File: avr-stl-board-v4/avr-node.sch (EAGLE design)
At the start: 36 parts, among them IC2 DS1307, IC3 LM358N, Q1 32.768kHz, Q3 16MHz, T1 S8050, U1 24LC256, U3 ATMEGA328P-PU

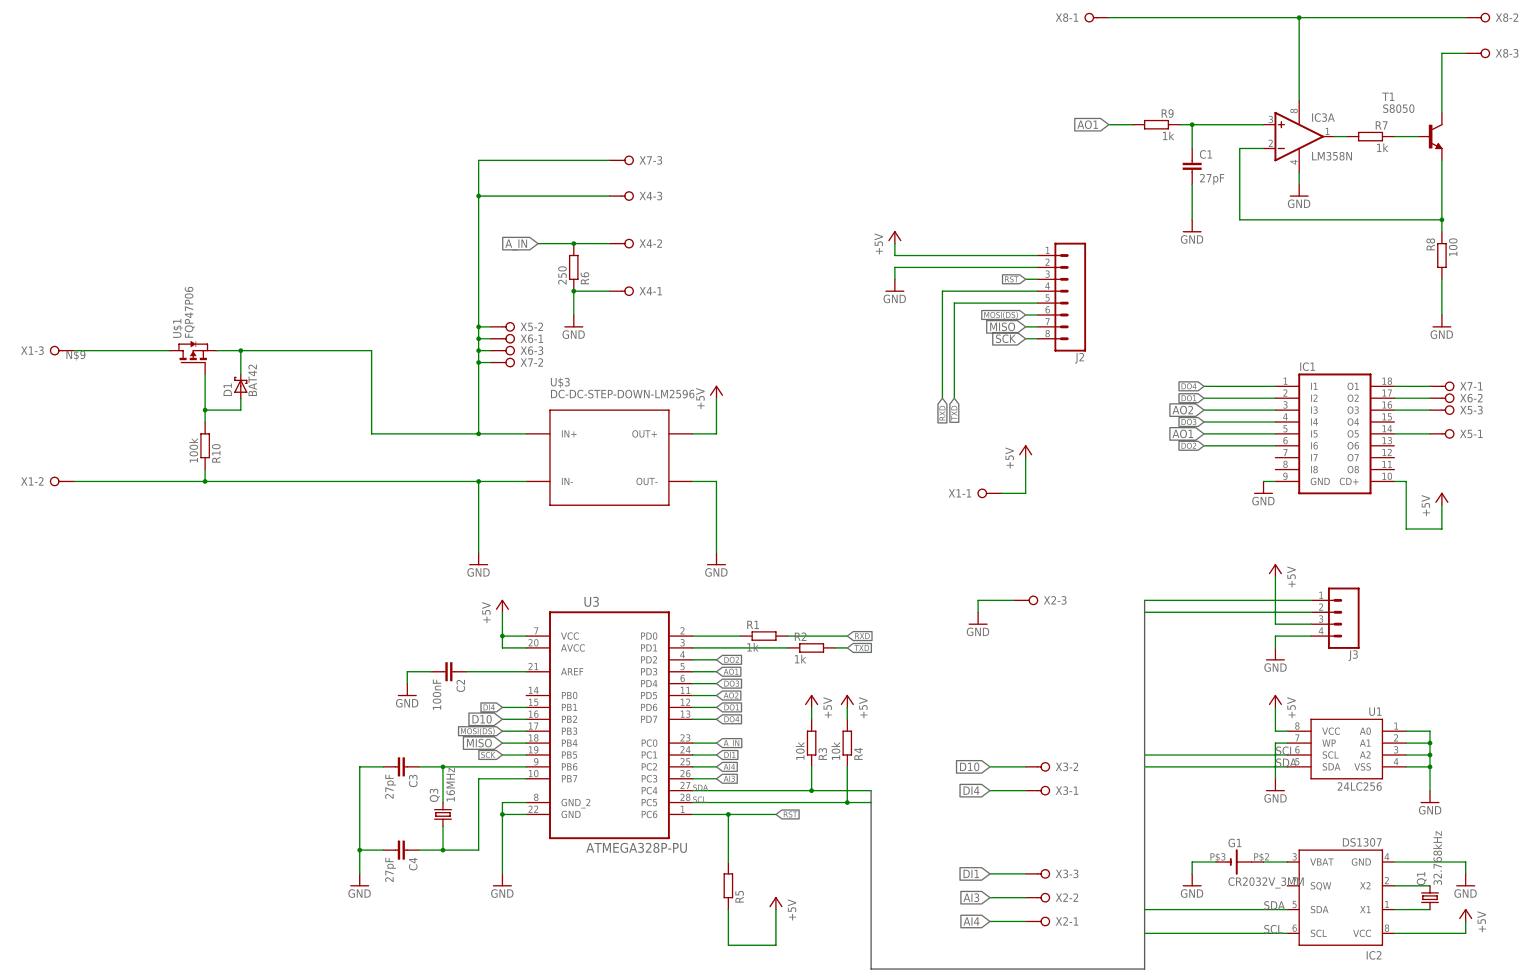
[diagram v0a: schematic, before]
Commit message: adding bit, byte, word persistant commands
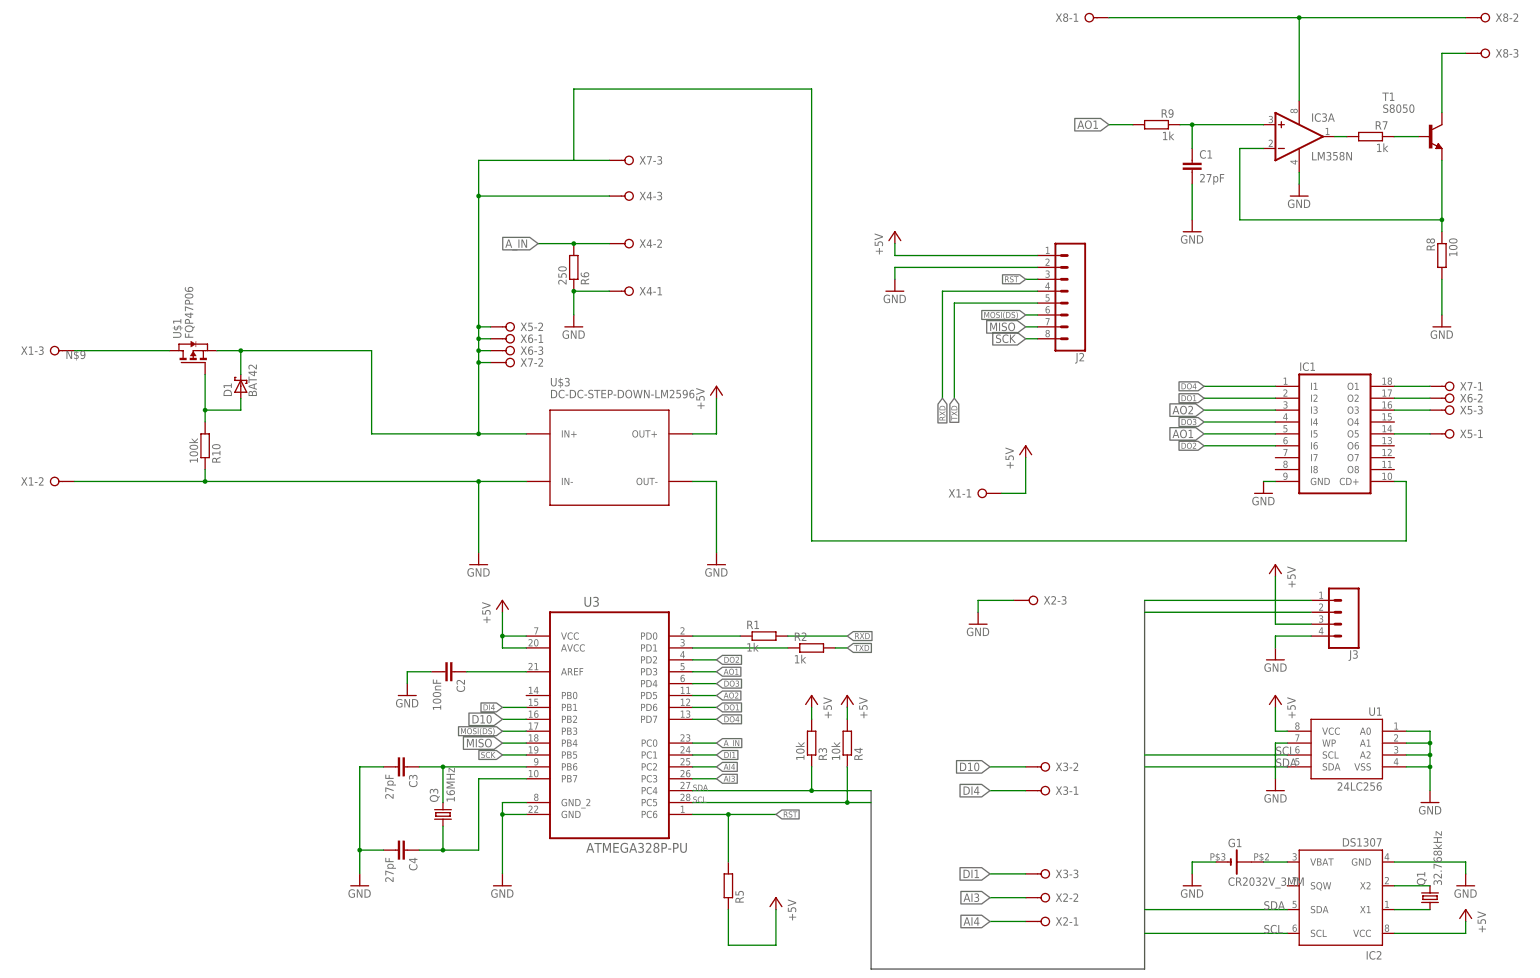
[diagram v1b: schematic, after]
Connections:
- net +5V: no longer IC1.CD+
- net V_IN: now also IC1.CD+
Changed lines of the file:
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@@
 <part name="R1" library="resistor" deviceset="R-EU_" device="0204/7" value="1k"/>
 <part name="R2" library="resistor" deviceset="R-EU_" device="0204/7" value="1k"/>
-<part name="P+2" library="supply1" deviceset="+5V" device=""/>
 <part name="GND2" library="supply1" deviceset="GND" device=""/>
 <part name="P+3" library="supply1" deviceset="+5V" device=""/>
@@
 <instance part="R1" gate="G$1" x="180.34" y="86.36"/>
 <instance part="R2" gate="G$1" x="190.5" y="83.82"/>
-<instance part="P+2" gate="1" x="325.12" y="116.84" smashed="yes">
-<attribute name="VALUE" x="322.58" y="111.76" size="1.778" layer="96" rot="R90"/>
-</instance>
 <instance part="GND2" gate="1" x="287.02" y="116.84" smashed="yes">
 <attribute name="VALUE" x="284.48" y="114.3" size="1.778" layer="96"/>
@@
 <wire x1="119.38" y1="180.34" x2="119.38" y2="187.96" width="0.1524" layer="91"/>
 <pinref part="X7" gate="-3" pin="KL"/>
-<wire x1="119.38" y1="187.96" x2="147.32" y2="187.96" width="0.1524" layer="91"/>
+<wire x1="119.38" y1="187.96" x2="139.7" y2="187.96" width="0.1524" layer="91"/>
 <junction x="119.38" y="180.34"/>
+<wire x1="139.7" y1="187.96" x2="147.32" y2="187.96" width="0.1524" layer="91"/>
 <wire x1="63.5" y1="147.32" x2="68.58" y2="147.32" width="0.1524" layer="91"/>
 <wire x1="68.58" y1="147.32" x2="96.52" y2="147.32" width="0.1524" layer="91"/>
@@
 <junction x="68.58" y="147.32"/>
 <pinref part="U$1" gate="G$1" pin="S"/>
+<wire x1="139.7" y1="187.96" x2="139.7" y2="203.2" width="0.1524" layer="91"/>
+<wire x1="139.7" y1="203.2" x2="190.5" y2="203.2" width="0.1524" layer="91"/>
+<wire x1="190.5" y1="203.2" x2="190.5" y2="106.68" width="0.1524" layer="91"/>
+<pinref part="IC1" gate="G$1" pin="CD+"/>
+<wire x1="314.96" y1="119.38" x2="317.5" y2="119.38" width="0.1524" layer="91"/>
+<wire x1="317.5" y1="119.38" x2="317.5" y2="106.68" width="0.1524" layer="91"/>
+<wire x1="190.5" y1="106.68" x2="317.5" y2="106.68" width="0.1524" layer="91"/>
 </segment>
 </net>
@@
 </segment>
 <segment>
-<pinref part="IC1" gate="G$1" pin="CD+"/>
-<wire x1="314.96" y1="119.38" x2="317.5" y2="119.38" width="0.1524" layer="91"/>
-<wire x1="317.5" y1="119.38" x2="317.5" y2="109.22" width="0.1524" layer="91"/>
-<pinref part="P+2" gate="1" pin="+5V"/>
-<wire x1="317.5" y1="109.22" x2="325.12" y2="109.22" width="0.1524" layer="91"/>
-<wire x1="325.12" y1="109.22" x2="325.12" y2="114.3" width="0.1524" layer="91"/>
-</segment>
-<segment>
